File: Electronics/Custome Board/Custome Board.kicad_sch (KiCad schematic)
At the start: 19 parts, among them J1 AVR ISP, SW1 Reset, SW2 Switch Mode, U1 ATMEGA328P-PU, Y1 16 MHz

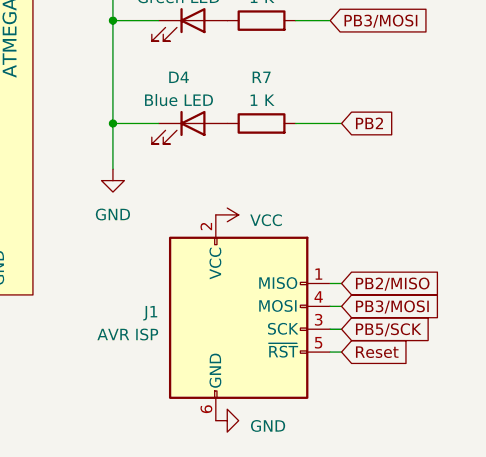
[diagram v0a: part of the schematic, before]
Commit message: schematic pinout err fixed
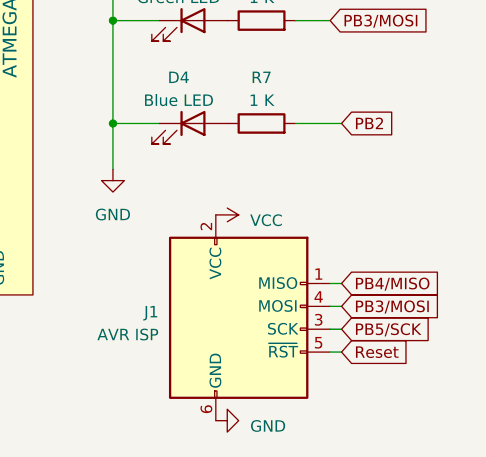
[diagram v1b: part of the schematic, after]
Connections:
- net PB2/MISO is gone; now on net PB4/MISO: J1.1 (MISO)
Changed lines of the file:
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@@
     )
   )
-  (global_label "PB2{slash}MISO" (shape input) (at 182.88 120.65 0) (fields_autoplaced)
+  (global_label "PB4{slash}MISO" (shape input) (at 182.88 120.65 0) (fields_autoplaced)
     (effects (font (size 1.27 1.27)) (justify left))
     (property "Intersheetrefs" "${INTERSHEET_REFS}" (at 195.462 120.65 0)
